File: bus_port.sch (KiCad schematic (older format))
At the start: 3 parts, among them P1 CONN_01X04, P1 CONN_01X40

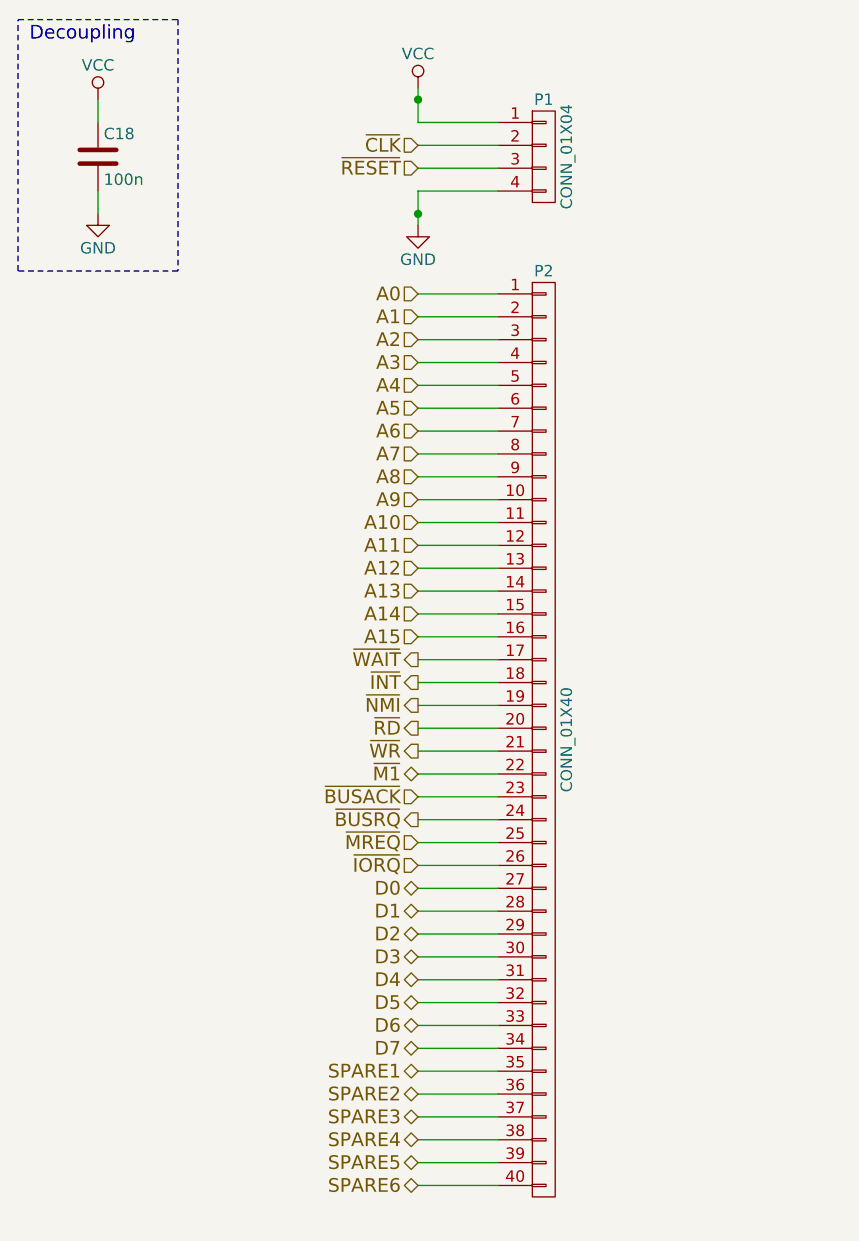
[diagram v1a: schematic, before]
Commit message: Added basic board layout WIP
Switched a few bus lines around to make the layout a little easier.
Still learning PCBNew, has a few quirks I haven't figured out yet.
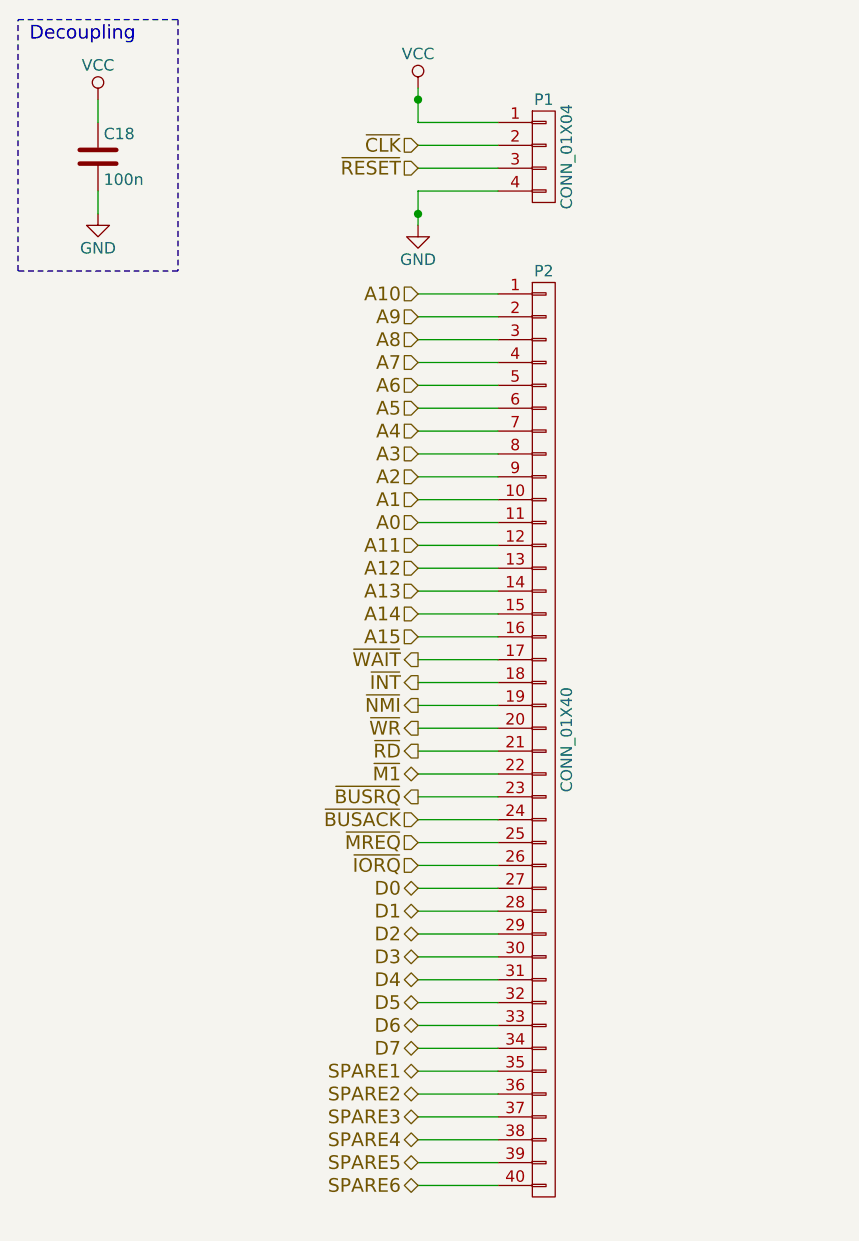
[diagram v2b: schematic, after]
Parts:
- C18: footprint Capacitors_SMD:C_1206_HandSoldering -> Capacitors_SMD:C_0805_HandSoldering
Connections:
- net A0: now also P1.11 (P11); no longer P1.1 (P1)
- net A1: now also P1.10 (P10); no longer P1.2 (P2)
- net A10: now also P1.1 (P1); no longer P1.11 (P11)
- net A2: now also P1.9 (P9); no longer P1.3 (P3)
- net A3: now also P1.8 (P8); no longer P1.4 (P4)
- net A4: now also P1.7 (P7); no longer P1.5 (P5)
- net A6: now also P1.5 (P5); no longer P1.7 (P7)
- net A7: now also P1.4 (P4); no longer P1.8 (P8)
- net A8: now also P1.3 (P3); no longer P1.9 (P9)
- net A9: now also P1.2 (P2); no longer P1.10 (P10)
- net ~BUSACK: now also P1.24 (P24); no longer P1.23 (P23)
- net ~BUSRQ: now also P1.23 (P23); no longer P1.24 (P24)
- net ~RD: now also P1.21 (P21); no longer P1.20 (P20)
- net ~WR: now also P1.20 (P20); no longer P1.21 (P21)
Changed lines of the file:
@@
 Comment4 ""
 $EndDescr
-Text HLabel 3900 2650 0    60   Input ~ 0
+Text HLabel 3900 3650 0    60   Input ~ 0
 A0
-Text HLabel 3900 2750 0    60   Input ~ 0
+Text HLabel 3900 3550 0    60   Input ~ 0
 A1
-Text HLabel 3900 2850 0    60   Input ~ 0
+Text HLabel 3900 3450 0    60   Input ~ 0
 A2
-Text HLabel 3900 2950 0    60   Input ~ 0
+Text HLabel 3900 3350 0    60   Input ~ 0
 A3
-Text HLabel 3900 3050 0    60   Input ~ 0
+Text HLabel 3900 3250 0    60   Input ~ 0
 A4
 Text HLabel 3900 3150 0    60   Input ~ 0
 A5
-Text HLabel 3900 3250 0    60   Input ~ 0
+Text HLabel 3900 3050 0    60   Input ~ 0
 A6
-Text HLabel 3900 3350 0    60   Input ~ 0
+Text HLabel 3900 2950 0    60   Input ~ 0
 A7
-Text HLabel 3900 3450 0    60   Input ~ 0
+Text HLabel 3900 2850 0    60   Input ~ 0
 A8
-Text HLabel 3900 3550 0    60   Input ~ 0
+Text HLabel 3900 2750 0    60   Input ~ 0
 A9
-Text HLabel 3900 3650 0    60   Input ~ 0
+Text HLabel 3900 2650 0    60   Input ~ 0
 A10
 Text HLabel 3900 3750 0    60   Input ~ 0
@@
 Text HLabel 3900 4350 0    60   Output ~ 0
 ~INT
+Text HLabel 3900 4650 0    60   Output ~ 0
+~RD
 Text HLabel 3900 4550 0    60   Output ~ 0
-~RD
-Text HLabel 3900 4650 0    60   Output ~ 0
 ~WR
 Text HLabel 3900 4750 0    60   3State ~ 0
 ~M1
-Text HLabel 3900 4850 0    60   Input ~ 0
+Text HLabel 3900 4950 0    60   Input ~ 0
 ~BUSACK
-Text HLabel 3900 4950 0    60   Output ~ 0
+Text HLabel 3900 4850 0    60   Output ~ 0
 ~BUSRQ
 Text HLabel 3900 5050 0    60   Input ~ 0
@@
 	3900 1750 3900 1900
 $Comp
-L VCC #PWR043
+L VCC #PWR046
 U 1 1 5781454A
 P 3900 1750
-AR Path="/577F17CE/577F1897/5781454A" Ref="#PWR043"  Part="1"
+AR Path="/577F17CE/577F1897/5781454A" Ref="#PWR046"  Part="1"
 AR Path="/577F17CE/577F7EB3/5781454A" Ref="#PWR019"  Part="1"
 AR Path="/577F17CE/577F8AF5/5781454A" Ref="#PWR021"  Part="1"
 AR Path="/577F17CE/577F9440/5781454A" Ref="#PWR023"  Part="1"
-AR Path="/577F17CE/5782F6B6/5781454A" Ref="#PWR047"  Part="1"
-AR Path="/577F17CE/5783136E/5781454A" Ref="#PWR051"  Part="1"
-AR Path="/577F17CE/57832B70/5781454A" Ref="#PWR055"  Part="1"
-F 0 "#PWR043" H 3900 1600 50  0001 C CNN
+AR Path="/577F17CE/5782F6B6/5781454A" Ref="#PWR050"  Part="1"
+AR Path="/577F17CE/5783136E/5781454A" Ref="#PWR054"  Part="1"
+AR Path="/577F17CE/57832B70/5781454A" Ref="#PWR058"  Part="1"
+F 0 "#PWR058" H 3900 1600 50  0001 C CNN
 F 1 "VCC" H 3900 1900 50  0000 C CNN
 F 2 "" H 3900 1750 50  0000 C CNN
@@
 	3900 2200 3900 2350
 $Comp
-L GND #PWR044
+L GND #PWR047
 U 1 1 5781458A
 P 3900 2350
-AR Path="/577F17CE/577F1897/5781458A" Ref="#PWR044"  Part="1"
+AR Path="/577F17CE/577F1897/5781458A" Ref="#PWR047"  Part="1"
 AR Path="/577F17CE/577F7EB3/5781458A" Ref="#PWR020"  Part="1"
 AR Path="/577F17CE/577F8AF5/5781458A" Ref="#PWR022"  Part="1"
 AR Path="/577F17CE/577F9440/5781458A" Ref="#PWR024"  Part="1"
-AR Path="/577F17CE/5782F6B6/5781458A" Ref="#PWR048"  Part="1"
-AR Path="/577F17CE/5783136E/5781458A" Ref="#PWR052"  Part="1"
-AR Path="/577F17CE/57832B70/5781458A" Ref="#PWR056"  Part="1"
-F 0 "#PWR044" H 3900 2100 50  0001 C CNN
+AR Path="/577F17CE/5782F6B6/5781458A" Ref="#PWR051"  Part="1"
+AR Path="/577F17CE/5783136E/5781458A" Ref="#PWR055"  Part="1"
+AR Path="/577F17CE/57832B70/5781458A" Ref="#PWR059"  Part="1"
+F 0 "#PWR059" H 3900 2100 50  0001 C CNN
 F 1 "GND" H 3900 2200 50  0000 C CNN
 F 2 "" H 3900 2350 50  0000 C CNN
@@
 F 0 "C18" H 2525 2150 50  0000 L CNN
 F 1 "100n" H 2525 1950 50  0000 L CNN
-F 2 "Capacitors_SMD:C_1206_HandSoldering" H 2538 1900 50  0001 C CNN
+F 2 "Capacitors_SMD:C_0805_HandSoldering" H 2538 1900 50  0001 C CNN
 F 3 "" H 2500 2050 50  0000 C CNN
 	1    2500 2050
@@
 Connection ~ 3900 2300
 $Comp
-L VCC #PWR045
+L VCC #PWR048
 U 1 1 5780D6F2
 P 2500 1800
-AR Path="/577F17CE/577F1897/5780D6F2" Ref="#PWR045"  Part="1"
-AR Path="/577F17CE/5782F6B6/5780D6F2" Ref="#PWR049"  Part="1"
-AR Path="/577F17CE/5783136E/5780D6F2" Ref="#PWR053"  Part="1"
-AR Path="/577F17CE/57832B70/5780D6F2" Ref="#PWR057"  Part="1"
-F 0 "#PWR045" H 2500 1650 50  0001 C CNN
+AR Path="/577F17CE/577F1897/5780D6F2" Ref="#PWR048"  Part="1"
+AR Path="/577F17CE/5782F6B6/5780D6F2" Ref="#PWR052"  Part="1"
+AR Path="/577F17CE/5783136E/5780D6F2" Ref="#PWR056"  Part="1"
+AR Path="/577F17CE/57832B70/5780D6F2" Ref="#PWR060"  Part="1"
+F 0 "#PWR060" H 2500 1650 50  0001 C CNN
 F 1 "VCC" H 2500 1950 50  0000 C CNN
 F 2 "" H 2500 1800 50  0000 C CNN
@@
 $EndComp
 $Comp
-L GND #PWR046
+L GND #PWR049
 U 1 1 5780D706
 P 2500 2300
-AR Path="/577F17CE/577F1897/5780D706" Ref="#PWR046"  Part="1"
-AR Path="/577F17CE/5782F6B6/5780D706" Ref="#PWR050"  Part="1"
-AR Path="/577F17CE/5783136E/5780D706" Ref="#PWR054"  Part="1"
-AR Path="/577F17CE/57832B70/5780D706" Ref="#PWR058"  Part="1"
-F 0 "#PWR046" H 2500 2050 50  0001 C CNN
+AR Path="/577F17CE/577F1897/5780D706" Ref="#PWR049"  Part="1"
+AR Path="/577F17CE/5782F6B6/5780D706" Ref="#PWR053"  Part="1"
+AR Path="/577F17CE/5783136E/5780D706" Ref="#PWR057"  Part="1"
+AR Path="/577F17CE/57832B70/5780D706" Ref="#PWR061"  Part="1"
+F 0 "#PWR061" H 2500 2050 50  0001 C CNN
 F 1 "GND" H 2500 2150 50  0000 C CNN
 F 2 "" H 2500 2300 50  0000 C CNN

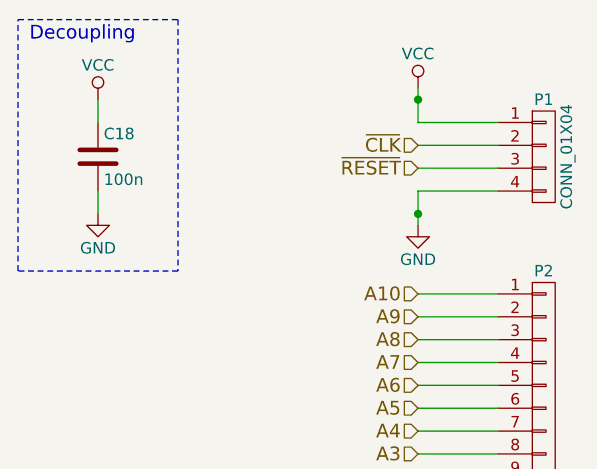
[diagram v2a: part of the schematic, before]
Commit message: Updated LEDs, added power supply options, added mounting holes in schematic.
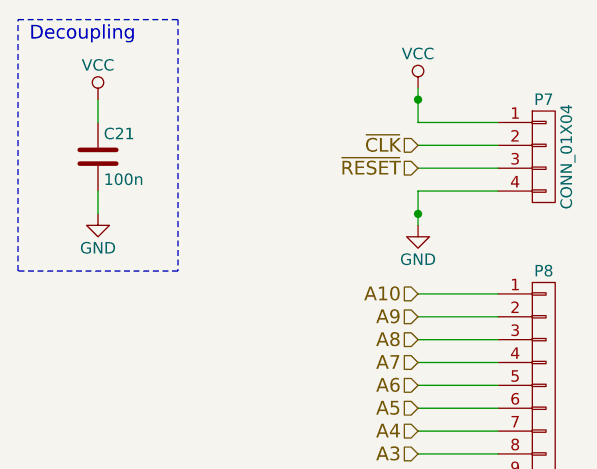
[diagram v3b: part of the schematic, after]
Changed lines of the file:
@@
 LIBS:microchip_pic18mcu
 LIBS:6850
+LIBS:nrc2016
 LIBS:z80-cache
 EELAYER 25 0
@@
 $Descr A4 11693 8268
 encoding utf-8
-Sheet 13 16
+Sheet 16 16
 Title ""
 Date ""
@@
 AR Path="/577F17CE/5783136E/577CEB68" Ref="P6"  Part="1"
 AR Path="/577F17CE/57832B70/577CEB68" Ref="P8"  Part="1"
-F 0 "P2" H 4450 6650 50  0000 C CNN
+F 0 "P8" H 4450 6650 50  0000 C CNN
 F 1 "CONN_01X40" V 4550 4600 50  0000 C CNN
 F 2 "Socket_Strips:Socket_Strip_Straight_1x40" H 4450 4600 50  0001 C CNN
@@
 AR Path="/577F17CE/5783136E/578144F7" Ref="P5"  Part="1"
 AR Path="/577F17CE/57832B70/578144F7" Ref="P7"  Part="1"
-F 0 "P1" H 4450 2300 50  0000 C CNN
+F 0 "P7" H 4450 2300 50  0000 C CNN
 F 1 "CONN_01X04" V 4550 2050 50  0000 C CNN
 F 2 "Pin_Headers:Pin_Header_Straight_1x04" H 4450 2050 50  0001 C CNN
@@
 AR Path="/577F17CE/5783136E/5780CE22" Ref="C20"  Part="1"
 AR Path="/577F17CE/57832B70/5780CE22" Ref="C21"  Part="1"
-F 0 "C18" H 2525 2150 50  0000 L CNN
+F 0 "C21" H 2525 2150 50  0000 L CNN
 F 1 "100n" H 2525 1950 50  0000 L CNN
 F 2 "Capacitors_SMD:C_0805_HandSoldering" H 2538 1900 50  0001 C CNN
